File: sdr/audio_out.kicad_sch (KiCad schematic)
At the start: 8 parts, among them U2 LM4871M/TR_C383075

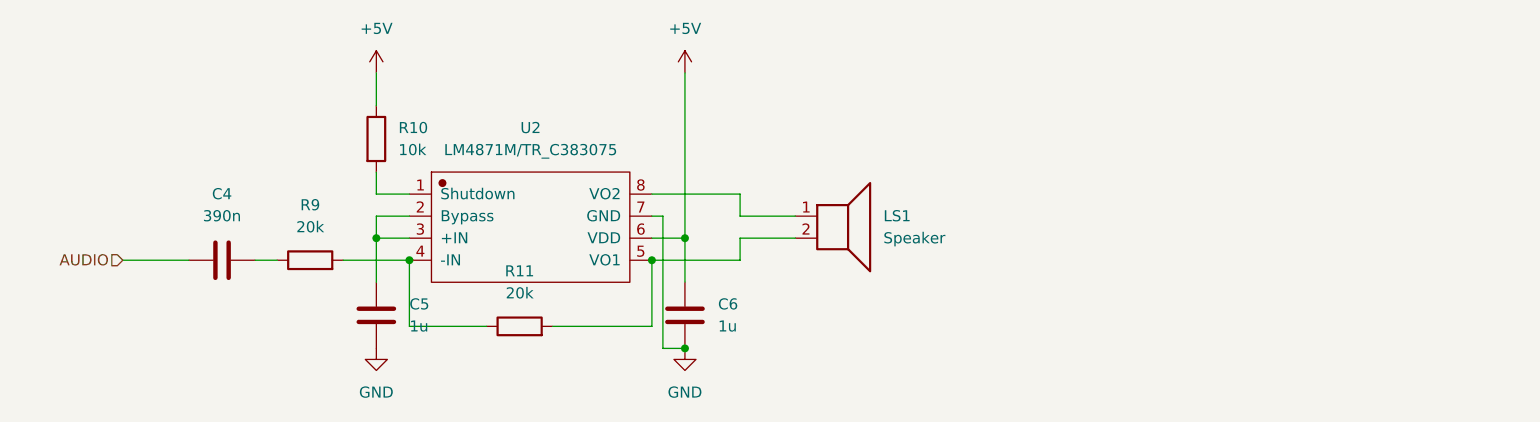
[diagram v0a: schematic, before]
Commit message: Update lots of things. Now have basic CPU as well as some crude mixers
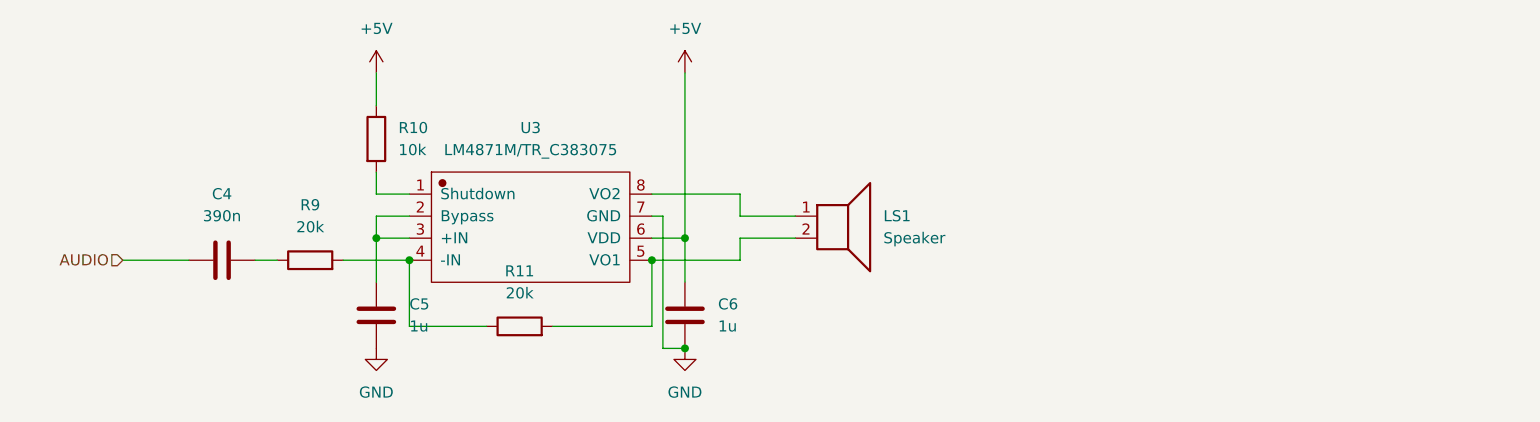
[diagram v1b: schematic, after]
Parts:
- renumbered U2 to U3
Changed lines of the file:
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@@
   (symbol (lib_id "zl4aa:LM4871M{slash}TR_C383075") (at 123.19 80.01 0) (unit 1)
     (in_bom yes) (on_board yes) (fields_autoplaced)
-    (property "Reference" "U2" (id 0) (at 123.19 68.58 0))
+    (property "Reference" "U3" (id 0) (at 123.19 68.58 0))
     (property "Value" "LM4871M/TR_C383075" (id 1) (at 123.19 71.12 0))
     (property "Footprint" "Package_SO:SOP-8_3.9x4.9mm_P1.27mm" (id 2) (at 123.19 68.58 0)
@@
   (symbol (lib_id "power:+5V") (at 105.41 62.23 0) (unit 1)
     (in_bom yes) (on_board yes) (fields_autoplaced)
-    (property "Reference" "#PWR011" (id 0) (at 105.41 66.04 0)
+    (property "Reference" "#PWR014" (id 0) (at 105.41 66.04 0)
       (effects (font (size 1.27 1.27)) hide)
     )
@@
   (symbol (lib_id "power:+5V") (at 140.97 62.23 0) (unit 1)
     (in_bom yes) (on_board yes) (fields_autoplaced)
-    (property "Reference" "#PWR013" (id 0) (at 140.97 66.04 0)
+    (property "Reference" "#PWR016" (id 0) (at 140.97 66.04 0)
       (effects (font (size 1.27 1.27)) hide)
     )
@@
   (symbol (lib_id "power:GND") (at 140.97 93.98 0) (unit 1)
     (in_bom yes) (on_board yes) (fields_autoplaced)
-    (property "Reference" "#PWR014" (id 0) (at 140.97 100.33 0)
+    (property "Reference" "#PWR017" (id 0) (at 140.97 100.33 0)
       (effects (font (size 1.27 1.27)) hide)
     )
@@
   (symbol (lib_id "power:GND") (at 105.41 93.98 0) (unit 1)
     (in_bom yes) (on_board yes) (fields_autoplaced)
-    (property "Reference" "#PWR012" (id 0) (at 105.41 100.33 0)
+    (property "Reference" "#PWR015" (id 0) (at 105.41 100.33 0)
       (effects (font (size 1.27 1.27)) hide)
     )

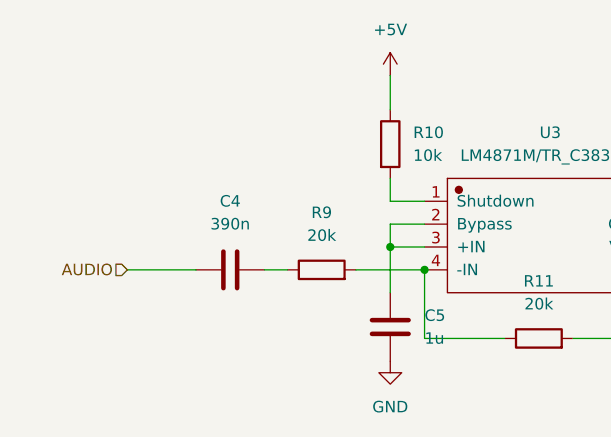
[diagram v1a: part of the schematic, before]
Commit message: Added ST-link 6-pin 0.1 programming header
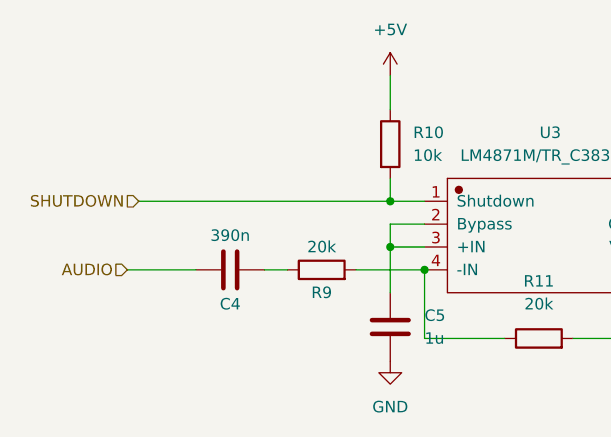
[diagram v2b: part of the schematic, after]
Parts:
- LS1: footprint (none) -> Resistor_SMD:R_0603_1608Metric
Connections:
- net SHUTDOWN: now reaches R10.2, U3.1 (Shutdown)
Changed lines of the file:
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@@
   (junction (at 140.97 93.98) (diameter 0) (color 0 0 0 0)
   )
+  (junction (at 105.41 76.2) (diameter 0) (color 0 0 0 0)
+  )
   (junction (at 140.97 81.28) (diameter 0) (color 0 0 0 0)
   )
@@
     (stroke (width 0) (type default) (color 0 0 0 0))
   )
+  (wire (pts (xy 77.47 76.2) (xy 105.41 76.2))
+    (stroke (width 0) (type default) (color 0 0 0 0))
+  )
   (wire (pts (xy 105.41 78.74) (xy 105.41 81.28))
     (stroke (width 0) (type default) (color 0 0 0 0))
@@
   (wire (pts (xy 140.97 62.23) (xy 140.97 81.28))
     (stroke (width 0) (type default) (color 0 0 0 0))
+  )
+  (hierarchical_label "SHUTDOWN" (shape input) (at 77.47 76.2 180)
+    (effects (font (size 1.27 1.27)) (justify right))
   )
   (hierarchical_label "AUDIO" (shape input) (at 76.2 83.82 180)
@@
       (effects (font (size 1.27 1.27)) (justify left))
     )
-    (property "Footprint" "" (id 2) (at 158.75 83.82 0)
+    (property "Footprint" "Resistor_SMD:R_0603_1608Metric" (id 2) (at 158.75 83.82 0)
       (effects (font (size 1.27 1.27)) hide)
     )
@@
   )
   (symbol (lib_id "Device:R") (at 97.79 83.82 90) (unit 1)
-    (in_bom yes) (on_board yes) (fields_autoplaced)
-    (property "Reference" "R9" (id 0) (at 97.79 77.47 90))
-    (property "Value" "20k" (id 1) (at 97.79 80.01 90))
+    (in_bom yes) (on_board yes)
+    (property "Reference" "R9" (id 0) (at 97.79 86.36 90))
+    (property "Value" "20k" (id 1) (at 97.79 81.28 90))
     (property "Footprint" "Resistor_SMD:R_0402_1005Metric" (id 2) (at 97.79 85.598 90)
       (effects (font (size 1.27 1.27)) hide)
@@
   )
   (symbol (lib_id "Device:C") (at 87.63 83.82 270) (unit 1)
-    (in_bom yes) (on_board yes) (fields_autoplaced)
-    (property "Reference" "C4" (id 0) (at 87.63 76.2 90))
-    (property "Value" "390n" (id 1) (at 87.63 78.74 90))
+    (in_bom yes) (on_board yes)
+    (property "Reference" "C4" (id 0) (at 87.63 87.63 90))
+    (property "Value" "390n" (id 1) (at 87.63 80.01 90))
     (property "Footprint" "Capacitor_SMD:C_0603_1608Metric" (id 2) (at 83.82 84.7852 0)
       (effects (font (size 1.27 1.27)) hide)

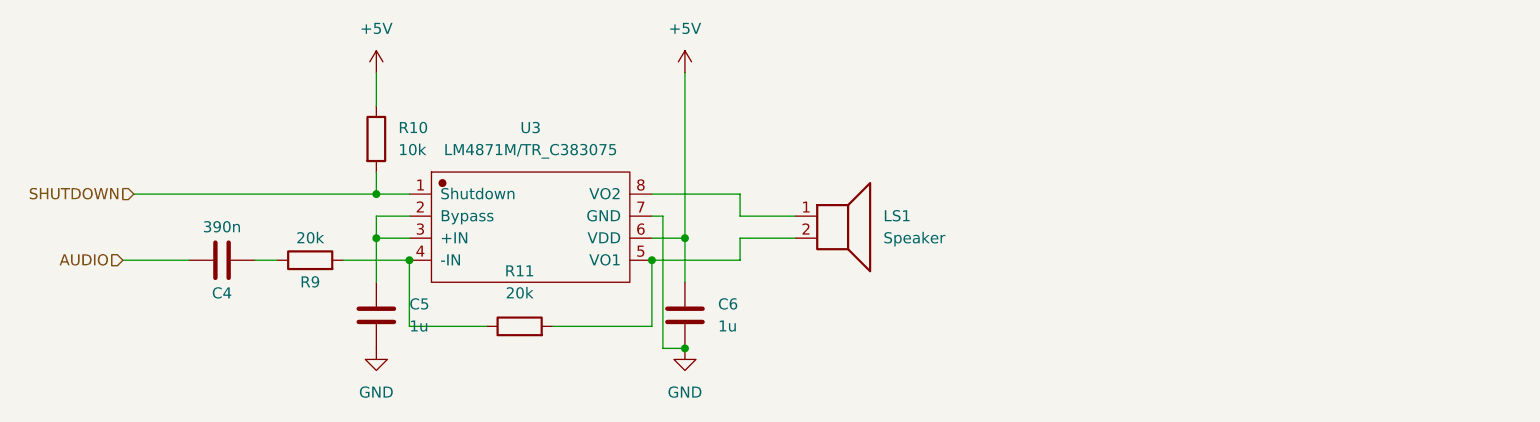
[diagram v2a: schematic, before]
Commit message: Tighten up design layout.
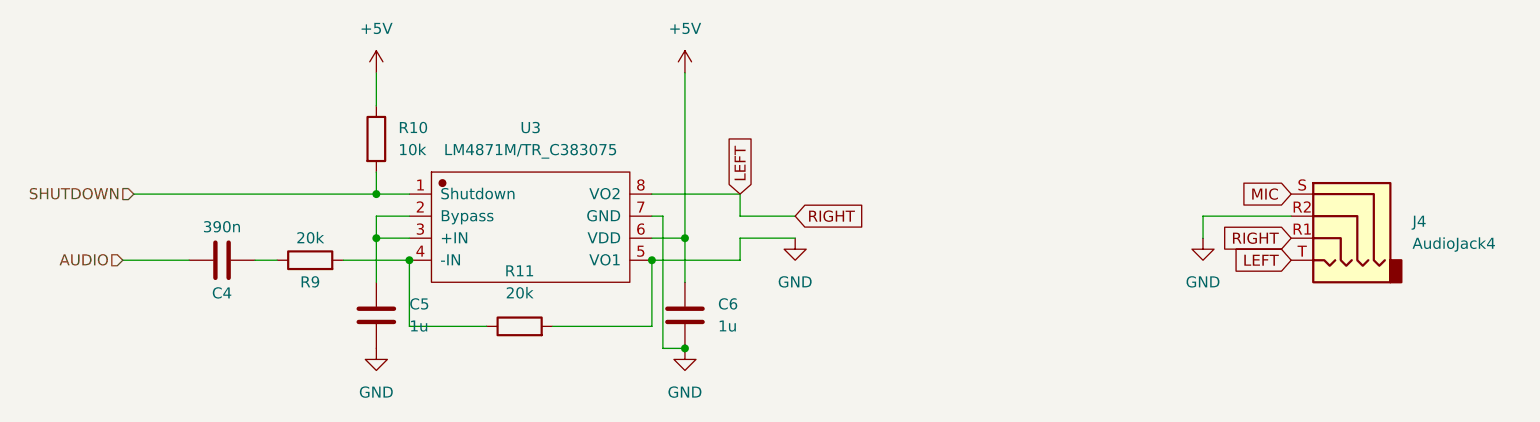
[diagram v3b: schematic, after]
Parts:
- removed LS1: Speaker, Resistor_SMD:R_0603_1608Metric, symbol Device:Speaker
- added J4: AudioJack4, Connector_Audio:Jack_3.5mm_PJ320D_Horizontal, symbol Connector:AudioJack4
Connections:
- net GND: now also R11.2, U3.5 (VO1), J4.R2
- net LEFT: now reaches U3.8 (VO2)
- net LEFT: now also J4.R1, J4.T
- new net MIC: J4.S
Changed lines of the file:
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@@
+    (stroke (width 0) (type default) (color 0 0 0 0))
+  )
+  (wire (pts (xy 210.82 78.74) (xy 200.66 78.74))
     (stroke (width 0) (type default) (color 0 0 0 0))
   )
@@
     (stroke (width 0) (type default) (color 0 0 0 0))
   )
+  (wire (pts (xy 200.66 78.74) (xy 200.66 81.28))
+    (stroke (width 0) (type default) (color 0 0 0 0))
+  )
   (wire (pts (xy 91.44 83.82) (xy 93.98 83.82))
     (stroke (width 0) (type default) (color 0 0 0 0))
@@
   (wire (pts (xy 140.97 62.23) (xy 140.97 81.28))
     (stroke (width 0) (type default) (color 0 0 0 0))
+  )
+  (global_label "LEFT" (shape input) (at 147.32 76.2 90) (fields_autoplaced)
+    (effects (font (size 1.27 1.27)) (justify left))
+    (property "Intersheet References" "${INTERSHEET_REFS}" (id 0) (at 147.3994 69.5536 90)
+      (effects (font (size 1.27 1.27)) (justify left) hide)
+    )
+  )
+  (global_label "RIGHT" (shape input) (at 210.82 81.28 180) (fields_autoplaced)
+    (effects (font (size 1.27 1.27)) (justify right))
+    (property "Intersheet References" "${INTERSHEET_REFS}" (id 0) (at 202.964 81.2006 0)
+      (effects (font (size 1.27 1.27)) (justify right) hide)
+    )
+  )
+  (global_label "LEFT" (shape input) (at 210.82 83.82 180) (fields_autoplaced)
+    (effects (font (size 1.27 1.27)) (justify right))
+    (property "Intersheet References" "${INTERSHEET_REFS}" (id 0) (at 204.1736 83.7406 0)
+      (effects (font (size 1.27 1.27)) (justify right) hide)
+    )
+  )
+  (global_label "MIC" (shape input) (at 210.82 76.2 180) (fields_autoplaced)
+    (effects (font (size 1.27 1.27)) (justify right))
+    (property "Intersheet References" "${INTERSHEET_REFS}" (id 0) (at 205.0807 76.1206 0)
+      (effects (font (size 1.27 1.27)) (justify right) hide)
+    )
+  )
+  (global_label "RIGHT" (shape input) (at 153.67 78.74 0) (fields_autoplaced)
+    (effects (font (size 1.27 1.27)) (justify left))
+    (property "Intersheet References" "${INTERSHEET_REFS}" (id 0) (at 161.526 78.6606 0)
+      (effects (font (size 1.27 1.27)) (justify left) hide)
+    )
   )
   (hierarchical_label "SHUTDOWN" (shape input) (at 77.47 76.2 180)
@@
     (pin "1")
   )
+  (symbol (lib_id "power:GND") (at 200.66 81.28 0) (unit 1)
+    (in_bom yes) (on_board yes) (fields_autoplaced)
+    (property "Reference" "#PWR0109" (id 0) (at 200.66 87.63 0)
+      (effects (font (size 1.27 1.27)) hide)
+    )
+    (property "Value" "GND" (id 1) (at 200.66 86.36 0))
+    (property "Footprint" "" (id 2) (at 200.66 81.28 0)
+      (effects (font (size 1.27 1.27)) hide)
+    )
+    (property "Datasheet" "" (id 3) (at 200.66 81.28 0)
+      (effects (font (size 1.27 1.27)) hide)
+    )
+    (pin "1")
+  )
+  (symbol (lib_id "Connector:AudioJack4") (at 215.9 78.74 0) (mirror y) (unit 1)
+    (in_bom yes) (on_board yes) (fields_autoplaced)
+    (property "Reference" "J4" (id 0) (at 224.79 79.3749 0)
+      (effects (font (size 1.27 1.27)) (justify right))
+    )
+    (property "Value" "AudioJack4" (id 1) (at 224.79 81.9149 0)
+      (effects (font (size 1.27 1.27)) (justify right))
+    )
+    (property "Footprint" "Connector_Audio:Jack_3.5mm_PJ320D_Horizontal" (id 2) (at 215.9 78.74 0)
+      (effects (font (size 1.27 1.27)) hide)
+    )
+    (property "Datasheet" "~" (id 3) (at 215.9 78.74 0)
+      (effects (font (size 1.27 1.27)) hide)
+    )
+    (pin "R1")
+    (pin "R2")
+    (pin "S")
+    (pin "T")
+  )
   (symbol (lib_id "Device:C") (at 105.41 90.17 0) (unit 1)
     (in_bom yes) (on_board yes) (fields_autoplaced)
@@
     (pin "2")
   )
-  (symbol (lib_id "Device:Speaker") (at 158.75 78.74 0) (unit 1)
-    (in_bom yes) (on_board yes) (fields_autoplaced)
-    (property "Reference" "LS1" (id 0) (at 163.83 78.7399 0)
-      (effects (font (size 1.27 1.27)) (justify left))
-    )
-    (property "Value" "Speaker" (id 1) (at 163.83 81.2799 0)
-      (effects (font (size 1.27 1.27)) (justify left))
-    )
-    (property "Footprint" "Resistor_SMD:R_0603_1608Metric" (id 2) (at 158.75 83.82 0)
-      (effects (font (size 1.27 1.27)) hide)
-    )
-    (property "Datasheet" "~" (id 3) (at 158.496 80.01 0)
-      (effects (font (size 1.27 1.27)) hide)
-    )
-    (property "LCSC" "C2847318" (id 4) (at 158.75 78.74 0)
-      (effects (font (size 1.27 1.27)) hide)
-    )
-    (pin "1")
-    (pin "2")
+  (symbol (lib_name "GND_1") (lib_id "power:GND") (at 153.67 81.28 0) (unit 1)
+    (in_bom yes) (on_board yes) (fields_autoplaced)
+    (property "Reference" "#PWR056" (id 0) (at 153.67 87.63 0)
+      (effects (font (size 1.27 1.27)) hide)
+    )
+    (property "Value" "GND" (id 1) (at 153.67 86.36 0))
+    (property "Footprint" "" (id 2) (at 153.67 81.28 0)
+      (effects (font (size 1.27 1.27)) hide)
+    )
+    (property "Datasheet" "" (id 3) (at 153.67 81.28 0)
+      (effects (font (size 1.27 1.27)) hide)
+    )
+    (pin "1")
   )
   (symbol (lib_id "power:+5V") (at 140.97 62.23 0) (unit 1)

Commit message: Many fixes. Updated mixers to use the analog switches rather than discretes.
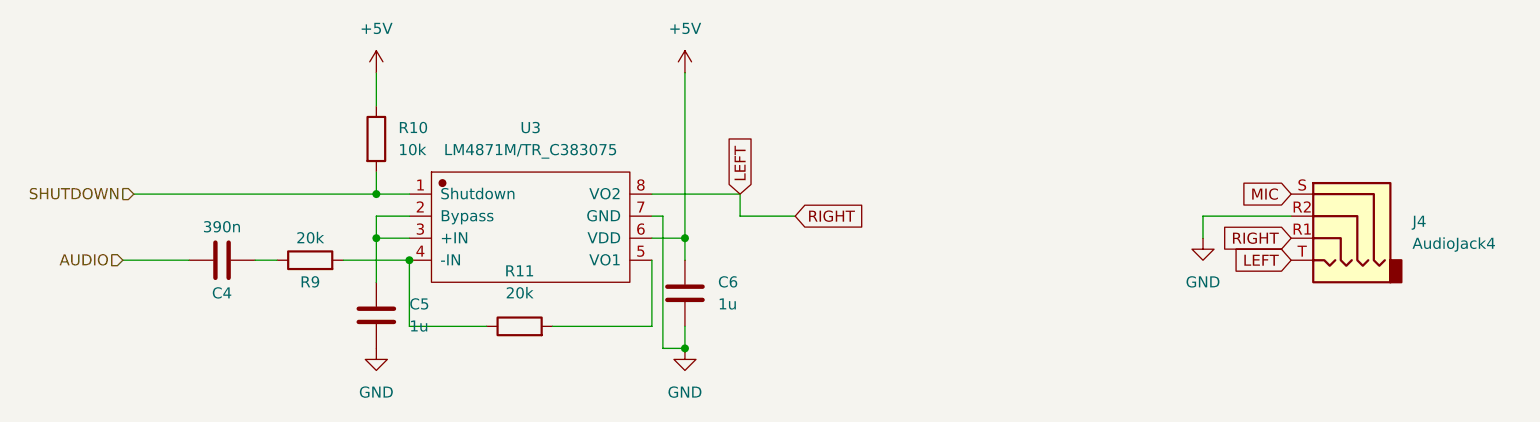
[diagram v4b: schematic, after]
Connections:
- net GND: no longer R11.2, U3.5 (VO1)
- new net: R11.2, U3.5 (VO1)
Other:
- moved on the sheet: C6
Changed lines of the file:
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@@
   (junction (at 140.97 81.28) (diameter 0) (color 0 0 0 0)
   )
-  (junction (at 137.16 83.82) (diameter 0) (color 0 0 0 0)
-  )
   (wire (pts (xy 118.11 91.44) (xy 109.22 91.44))
     (stroke (width 0) (type default) (color 0 0 0 0))
@@
     (stroke (width 0) (type default) (color 0 0 0 0))
   )
-  (wire (pts (xy 147.32 81.28) (xy 147.32 83.82))
-    (stroke (width 0) (type default) (color 0 0 0 0))
-  )
   (wire (pts (xy 210.82 78.74) (xy 200.66 78.74))
     (stroke (width 0) (type default) (color 0 0 0 0))
@@
     (stroke (width 0) (type default) (color 0 0 0 0))
   )
-  (wire (pts (xy 140.97 86.36) (xy 140.97 81.28))
+  (wire (pts (xy 140.97 83.82) (xy 140.97 81.28))
+    (stroke (width 0) (type default) (color 0 0 0 0))
+  )
+  (wire (pts (xy 140.97 91.44) (xy 140.97 93.98))
     (stroke (width 0) (type default) (color 0 0 0 0))
   )
@@
   )
   (wire (pts (xy 105.41 62.23) (xy 105.41 66.04))
-    (stroke (width 0) (type default) (color 0 0 0 0))
-  )
-  (wire (pts (xy 153.67 81.28) (xy 147.32 81.28))
-    (stroke (width 0) (type default) (color 0 0 0 0))
-  )
-  (wire (pts (xy 147.32 83.82) (xy 137.16 83.82))
     (stroke (width 0) (type default) (color 0 0 0 0))
   )
@@
     (pin "2")
   )
-  (symbol (lib_name "GND_1") (lib_id "power:GND") (at 153.67 81.28 0) (unit 1)
-    (in_bom yes) (on_board yes) (fields_autoplaced)
-    (property "Reference" "#PWR056" (id 0) (at 153.67 87.63 0)
-      (effects (font (size 1.27 1.27)) hide)
-    )
-    (property "Value" "GND" (id 1) (at 153.67 86.36 0))
-    (property "Footprint" "" (id 2) (at 153.67 81.28 0)
-      (effects (font (size 1.27 1.27)) hide)
-    )
-    (property "Datasheet" "" (id 3) (at 153.67 81.28 0)
-      (effects (font (size 1.27 1.27)) hide)
-    )
-    (pin "1")
-  )
   (symbol (lib_id "power:+5V") (at 140.97 62.23 0) (unit 1)
     (in_bom yes) (on_board yes) (fields_autoplaced)
@@
     (pin "2")
   )
-  (symbol (lib_id "Device:C") (at 140.97 90.17 0) (unit 1)
-    (in_bom yes) (on_board yes) (fields_autoplaced)
-    (property "Reference" "C6" (id 0) (at 144.78 88.8999 0)
-      (effects (font (size 1.27 1.27)) (justify left))
-    )
-    (property "Value" "1u" (id 1) (at 144.78 91.4399 0)
-      (effects (font (size 1.27 1.27)) (justify left))
-    )
-    (property "Footprint" "Capacitor_SMD:C_0603_1608Metric" (id 2) (at 141.9352 93.98 0)
-      (effects (font (size 1.27 1.27)) hide)
-    )
-    (property "Datasheet" "~" (id 3) (at 140.97 90.17 0)
-      (effects (font (size 1.27 1.27)) hide)
-    )
+  (symbol (lib_id "Device:C") (at 140.97 87.63 0) (unit 1)
+    (in_bom yes) (on_board yes) (fields_autoplaced)
+    (property "Reference" "C6" (id 0) (at 144.78 86.3599 0)
+      (effects (font (size 1.27 1.27)) (justify left))
+    )
+    (property "Value" "1u" (id 1) (at 144.78 88.8999 0)
+      (effects (font (size 1.27 1.27)) (justify left))
+    )
+    (property "Footprint" "Capacitor_SMD:C_0603_1608Metric" (id 2) (at 141.9352 91.44 0)
+      (effects (font (size 1.27 1.27)) hide)
+    )
+    (property "Datasheet" "~" (id 3) (at 140.97 87.63 0)
+      (effects (font (size 1.27 1.27)) hide)
+    )
